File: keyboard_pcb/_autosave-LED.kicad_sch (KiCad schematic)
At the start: 87 parts

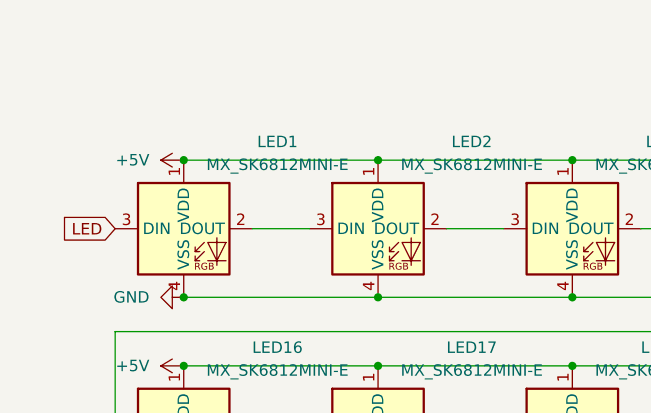
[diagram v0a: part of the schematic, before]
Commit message: reworked board outline
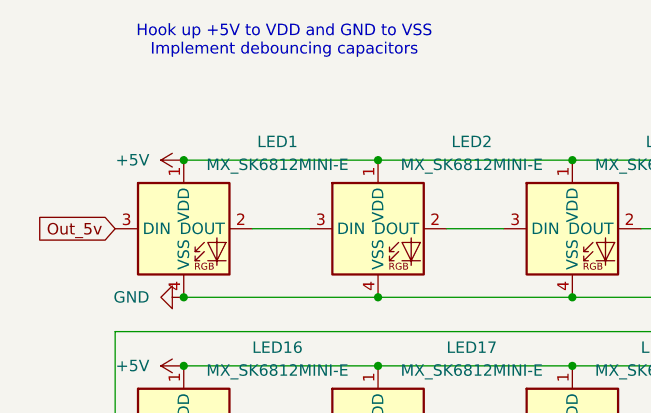
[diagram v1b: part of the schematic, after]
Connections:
- net LED renamed Out_5v
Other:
- note added: "Hook up +5V to VDD and GND to VSS Implement debouncing capacitors"
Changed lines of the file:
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@@
 		)
 	)
-	(global_label "LED"
+	(text "Hook up +5V to VDD and GND to VSS\nImplement debouncing capacitors"
+		(exclude_from_sim no)
+		(at 59.436 19.812 0)
+		(effects
+			(font
+				(size 1.27 1.27)
+			)
+		)
+	)
+	(global_label "Out_5v"
 		(shape input)
 		(at 40.64 40.64 180)
@@
 		)
 		(property "Intersheetrefs" "${INTERSHEET_REFS}"
-			(at 34.2077 40.64 0)
+			(at 31.3049 40.64 0)
 			(effects
 				(font
